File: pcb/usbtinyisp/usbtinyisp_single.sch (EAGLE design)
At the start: 23 parts, among them IC1 ATTINY2313-20P, IC2 74LVX125D, Q1 12000

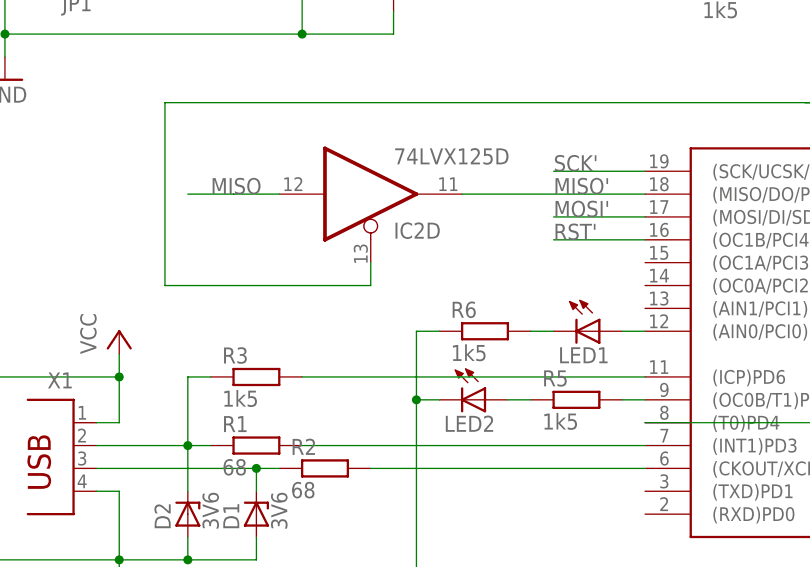
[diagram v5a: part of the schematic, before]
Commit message: swap LED1 with resistor
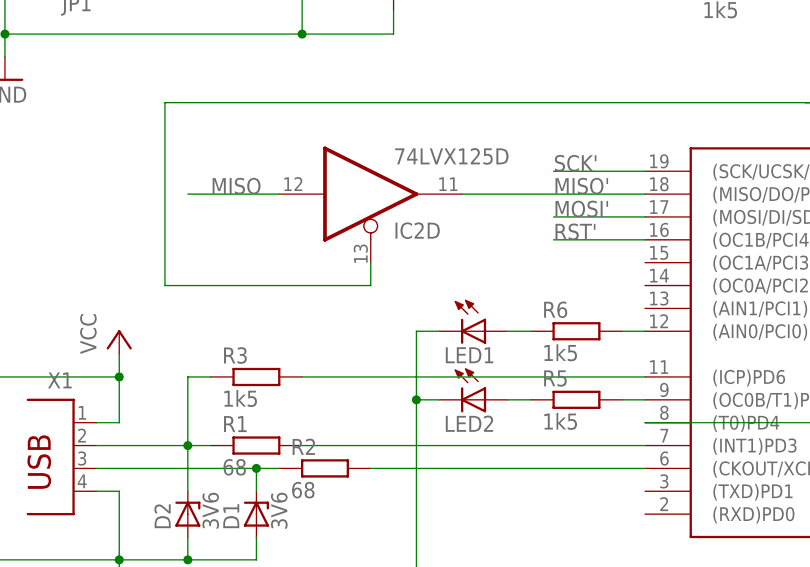
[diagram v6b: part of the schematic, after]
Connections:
- removed net N$8: LED1.C, R6.2
- new net N$5: LED1.A, R6.1
- net GND: now also LED1.C; no longer R6.1
- net N$7: now also R6.2; no longer LED1.A
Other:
- moved on the sheet: LED1, R6
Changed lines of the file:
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@@
 <grid distance="0.1" unitdist="inch" unit="inch" style="lines" multiple="1" display="no" altdistance="0.01" altunitdist="inch" altunit="inch"/>
 <layers>
-<layer number="1" name="Top" color="4" fill="1" visible="yes" active="no"/>
-<layer number="2" name="Route2" color="1" fill="3" visible="yes" active="no"/>
-<layer number="3" name="Route3" color="4" fill="3" visible="yes" active="no"/>
-<layer number="4" name="Route4" color="1" fill="4" visible="yes" active="no"/>
-<layer number="5" name="Route5" color="4" fill="4" visible="yes" active="no"/>
-<layer number="6" name="Route6" color="1" fill="8" visible="yes" active="no"/>
-<layer number="7" name="Route7" color="4" fill="8" visible="yes" active="no"/>
-<layer number="8" name="Route8" color="1" fill="2" visible="yes" active="no"/>
-<layer number="9" name="Route9" color="4" fill="2" visible="yes" active="no"/>
-<layer number="10" name="Route10" color="1" fill="7" visible="yes" active="no"/>
-<layer number="11" name="Route11" color="4" fill="7" visible="yes" active="no"/>
-<layer number="12" name="Route12" color="1" fill="5" visible="yes" active="no"/>
-<layer number="13" name="Route13" color="4" fill="5" visible="yes" active="no"/>
-<layer number="14" name="Route14" color="1" fill="6" visible="yes" active="no"/>
-<layer number="15" name="Route15" color="4" fill="6" visible="yes" active="no"/>
-<layer number="16" name="Bottom" color="1" fill="1" visible="yes" active="no"/>
-<layer number="17" name="Pads" color="2" fill="1" visible="yes" active="no"/>
-<layer number="18" name="Vias" color="2" fill="1" visible="yes" active="no"/>
-<layer number="19" name="Unrouted" color="6" fill="1" visible="yes" active="no"/>
-<layer number="20" name="Dimension" color="15" fill="1" visible="yes" active="no"/>
-<layer number="21" name="tPlace" color="7" fill="1" visible="yes" active="no"/>
-<layer number="22" name="bPlace" color="7" fill="1" visible="yes" active="no"/>
-<layer number="23" name="tOrigins" color="15" fill="1" visible="yes" active="no"/>
-<layer number="24" name="bOrigins" color="15" fill="1" visible="yes" active="no"/>
-<layer number="25" name="tNames" color="7" fill="1" visible="yes" active="no"/>
-<layer number="26" name="bNames" color="7" fill="1" visible="yes" active="no"/>
-<layer number="27" name="tValues" color="7" fill="1" visible="yes" active="no"/>
-<layer number="28" name="bValues" color="7" fill="1" visible="yes" active="no"/>
+<layer number="1" name="Top" color="4" fill="1" visible="no" active="no"/>
+<layer number="2" name="Route2" color="1" fill="3" visible="no" active="no"/>
+<layer number="3" name="Route3" color="4" fill="3" visible="no" active="no"/>
+<layer number="4" name="Route4" color="1" fill="4" visible="no" active="no"/>
+<layer number="5" name="Route5" color="4" fill="4" visible="no" active="no"/>
+<layer number="6" name="Route6" color="1" fill="8" visible="no" active="no"/>
+<layer number="7" name="Route7" color="4" fill="8" visible="no" active="no"/>
+<layer number="8" name="Route8" color="1" fill="2" visible="no" active="no"/>
+<layer number="9" name="Route9" color="4" fill="2" visible="no" active="no"/>
+<layer number="10" name="Route10" color="1" fill="7" visible="no" active="no"/>
+<layer number="11" name="Route11" color="4" fill="7" visible="no" active="no"/>
+<layer number="12" name="Route12" color="1" fill="5" visible="no" active="no"/>
+<layer number="13" name="Route13" color="4" fill="5" visible="no" active="no"/>
+<layer number="14" name="Route14" color="1" fill="6" visible="no" active="no"/>
+<layer number="15" name="Route15" color="4" fill="6" visible="no" active="no"/>
+<layer number="16" name="Bottom" color="1" fill="1" visible="no" active="no"/>
+<layer number="17" name="Pads" color="2" fill="1" visible="no" active="no"/>
+<layer number="18" name="Vias" color="2" fill="1" visible="no" active="no"/>
+<layer number="19" name="Unrouted" color="6" fill="1" visible="no" active="no"/>
+<layer number="20" name="Dimension" color="15" fill="1" visible="no" active="no"/>
+<layer number="21" name="tPlace" color="7" fill="1" visible="no" active="no"/>
+<layer number="22" name="bPlace" color="7" fill="1" visible="no" active="no"/>
+<layer number="23" name="tOrigins" color="15" fill="1" visible="no" active="no"/>
+<layer number="24" name="bOrigins" color="15" fill="1" visible="no" active="no"/>
+<layer number="25" name="tNames" color="7" fill="1" visible="no" active="no"/>
+<layer number="26" name="bNames" color="7" fill="1" visible="no" active="no"/>
+<layer number="27" name="tValues" color="7" fill="1" visible="no" active="no"/>
+<layer number="28" name="bValues" color="7" fill="1" visible="no" active="no"/>
 <layer number="29" name="tStop" color="7" fill="3" visible="no" active="no"/>
 <layer number="30" name="bStop" color="7" fill="6" visible="no" active="no"/>
@@
 <layer number="35" name="tGlue" color="7" fill="4" visible="no" active="no"/>
 <layer number="36" name="bGlue" color="7" fill="5" visible="no" active="no"/>
-<layer number="37" name="tTest" color="7" fill="1" visible="yes" active="no"/>
-<layer number="38" name="bTest" color="7" fill="1" visible="yes" active="no"/>
+<layer number="37" name="tTest" color="7" fill="1" visible="no" active="no"/>
+<layer number="38" name="bTest" color="7" fill="1" visible="no" active="no"/>
 <layer number="39" name="tKeepout" color="4" fill="11" visible="no" active="no"/>
 <layer number="40" name="bKeepout" color="1" fill="11" visible="no" active="no"/>
@@
 <layer number="44" name="Drills" color="7" fill="1" visible="no" active="no"/>
 <layer number="45" name="Holes" color="7" fill="1" visible="no" active="no"/>
-<layer number="46" name="Milling" color="3" fill="1" visible="yes" active="no"/>
-<layer number="47" name="Measures" color="7" fill="1" visible="yes" active="no"/>
-<layer number="48" name="Document" color="7" fill="1" visible="yes" active="no"/>
-<layer number="49" name="Reference" color="7" fill="1" visible="yes" active="no"/>
-<layer number="50" name="dxf" color="7" fill="1" visible="yes" active="no"/>
-<layer number="51" name="tDocu" color="7" fill="1" visible="yes" active="no"/>
-<layer number="52" name="bDocu" color="7" fill="1" visible="yes" active="no"/>
+<layer number="46" name="Milling" color="3" fill="1" visible="no" active="no"/>
+<layer number="47" name="Measures" color="7" fill="1" visible="no" active="no"/>
+<layer number="48" name="Document" color="7" fill="1" visible="no" active="no"/>
+<layer number="49" name="Reference" color="7" fill="1" visible="no" active="no"/>
+<layer number="50" name="dxf" color="7" fill="1" visible="no" active="no"/>
+<layer number="51" name="tDocu" color="7" fill="1" visible="no" active="no"/>
+<layer number="52" name="bDocu" color="7" fill="1" visible="no" active="no"/>
 <layer number="91" name="Nets" color="2" fill="1" visible="yes" active="yes"/>
 <layer number="92" name="Busses" color="1" fill="1" visible="yes" active="yes"/>
@@
 <instance part="C1" gate="G$1" x="152.4" y="86.36"/>
 <instance part="P+1" gate="VCC" x="25.4" y="91.44"/>
-<instance part="LED1" gate="G$1" x="78.74" y="91.44" rot="R270"/>
-<instance part="R6" gate="G$1" x="66.04" y="91.44"/>
+<instance part="LED1" gate="G$1" x="66.04" y="91.44" rot="R270"/>
+<instance part="R6" gate="G$1" x="76.2" y="91.44"/>
 <instance part="GND5" gate="1" x="58.42" y="60.96"/>
 <instance part="D1" gate="G$1" x="40.64" y="71.12" rot="R90"/>
@@
 <segment>
 <wire x1="60.96" y1="83.82" x2="58.42" y2="83.82" width="0.1524" layer="91"/>
-<wire x1="60.96" y1="91.44" x2="58.42" y2="91.44" width="0.1524" layer="91"/>
 <wire x1="58.42" y1="91.44" x2="58.42" y2="83.82" width="0.1524" layer="91"/>
 <pinref part="GND5" gate="1" pin="GND"/>
 <pinref part="LED2" gate="G$1" pin="C"/>
-<pinref part="R6" gate="G$1" pin="1"/>
 <junction x="58.42" y="83.82"/>
 <wire x1="58.42" y1="83.82" x2="58.42" y2="63.5" width="0.1524" layer="91"/>
+<pinref part="LED1" gate="G$1" pin="C"/>
+<wire x1="58.42" y1="91.44" x2="60.96" y2="91.44" width="0.1524" layer="91"/>
 </segment>
 <segment>
@@
 <net name="MISO" class="0">
 <segment>
-<wire x1="33.02" y1="106.68" x2="38.1" y2="106.68" width="0.1524" layer="91"/>
 <label x="35.56" y="106.68" size="1.778" layer="95"/>
+<pinref part="IC2" gate="D" pin="I"/>
+<wire x1="43.18" y1="106.68" x2="33.02" y2="106.68" width="0.1524" layer="91"/>
 </segment>
 <segment>
@@
 <pinref part="JP1" gate="1" pin="1"/>
 </segment>
-<segment>
-<pinref part="IC2" gate="D" pin="I"/>
-<wire x1="43.18" y1="106.68" x2="38.1" y2="106.68" width="0.1524" layer="91"/>
-</segment>
 </net>
 <net name="SCK" class="0">
@@
 <pinref part="LED2" gate="G$1" pin="A"/>
 <pinref part="R5" gate="G$1" pin="1"/>
-</segment>
-</net>
-<net name="N$7" class="0">
-<segment>
-<pinref part="IC1" gate="G$1" pin="(AIN0/PCI0)PB0"/>
-<pinref part="LED1" gate="G$1" pin="A"/>
-<wire x1="81.28" y1="91.44" x2="83.82" y2="91.44" width="0.1524" layer="91"/>
-</segment>
-</net>
-<net name="N$8" class="0">
-<segment>
-<wire x1="71.12" y1="91.44" x2="73.66" y2="91.44" width="0.1524" layer="91"/>
-<pinref part="R6" gate="G$1" pin="2"/>
-<pinref part="LED1" gate="G$1" pin="C"/>
 </segment>
 </net>
@@
 </segment>
 </net>
+<net name="N$5" class="0">
+<segment>
+<pinref part="LED1" gate="G$1" pin="A"/>
+<pinref part="R6" gate="G$1" pin="1"/>
+<wire x1="68.58" y1="91.44" x2="71.12" y2="91.44" width="0.1524" layer="91"/>
+</segment>
+</net>
+<net name="N$7" class="0">
+<segment>
+<pinref part="R6" gate="G$1" pin="2"/>
+<pinref part="IC1" gate="G$1" pin="(AIN0/PCI0)PB0"/>
+<wire x1="81.28" y1="91.44" x2="83.82" y2="91.44" width="0.1524" layer="91"/>
+</segment>
+</net>
